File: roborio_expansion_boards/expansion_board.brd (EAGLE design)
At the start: 55.9 x 88.9 mm, 19 parts

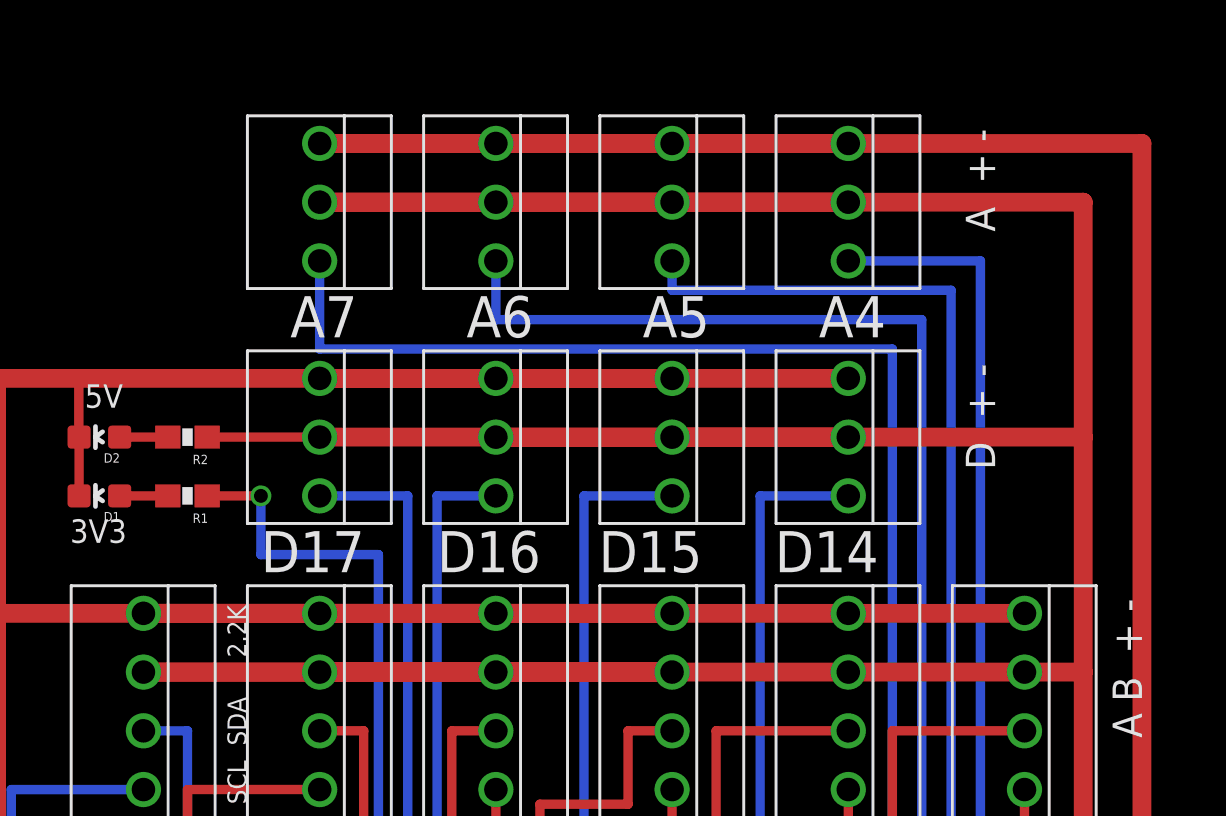
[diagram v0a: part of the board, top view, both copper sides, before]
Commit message: added capacitors to the power lines near each connector
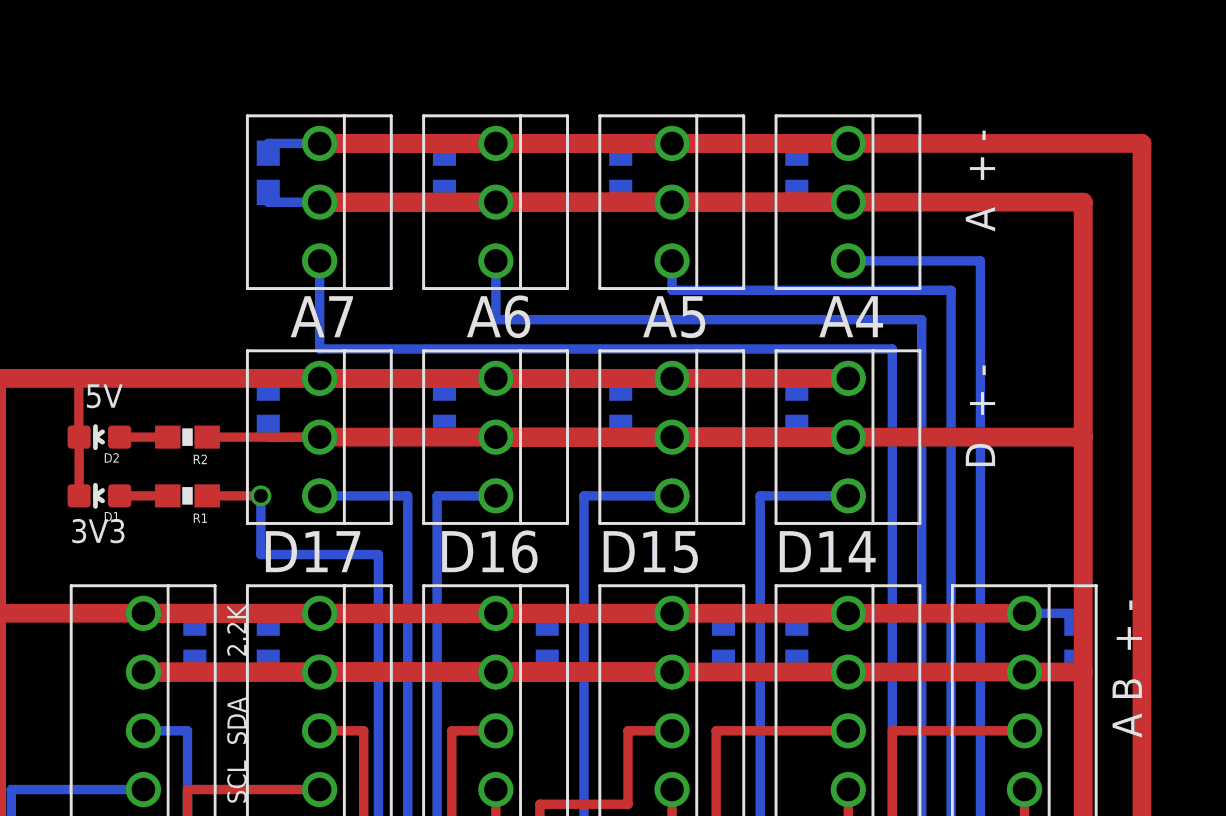
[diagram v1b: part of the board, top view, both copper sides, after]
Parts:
- added C1, C10, C11, C12, C13, C14, C2, C3, C4, C5, C6, C7, C8, C9: (no value), custom:0603
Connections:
- net 5V: now also C1.1, C10.2, C11.2, C12.2, C13.2, C14.2, C2.1, C3.1, C4.1, C5.1, C6.1, C7.2, C8.2, C9.2
- net AGND: now also C11.1, C12.1, C13.1, C14.1
- net DGND: now also C1.2, C10.1, C2.2, C3.2, C4.2, C5.2, C6.2, C7.1, C8.1, C9.1
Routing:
- net 5V: track 246.2 -> 283.2 mm
- net DGND: track 241.9 -> 268.4 mm
- net AGND: track 127.0 -> 137.6 mm
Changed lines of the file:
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@@
 <setting verticaltext="up"/>
 </settings>
-<grid distance="0.025" unitdist="inch" unit="inch" style="lines" multiple="1" display="no" altdistance="0.001" altunitdist="inch" altunit="inch"/>
+<grid distance="0.0125" unitdist="inch" unit="inch" style="lines" multiple="1" display="no" altdistance="0.001" altunitdist="inch" altunit="inch"/>
 <layers>
 <layer number="1" name="Top" color="4" fill="1" visible="yes" active="yes"/>
@@
 </element>
 <element name="R2" library="SparkFun-Passives" package="0603-RES" value="150" x="10.795" y="34.29" rot="R180"/>
+<element name="C1" library="custom" package="0603" value="" x="49.2125" y="25.4" rot="MR90"/>
+<element name="C2" library="custom" package="0603" value="" x="37.1475" y="25.4" rot="MR90"/>
+<element name="C3" library="custom" package="0603" value="" x="33.9725" y="25.4" rot="MR90"/>
+<element name="C4" library="custom" package="0603" value="" x="26.3525" y="25.4" rot="MR90"/>
+<element name="C5" library="custom" package="0603" value="" x="14.2875" y="25.4" rot="MR90"/>
+<element name="C6" library="custom" package="0603" value="" x="11.1125" y="25.4" rot="MR90"/>
+<element name="C7" library="custom" package="0603" value="" x="14.2875" y="35.56" rot="MR270"/>
+<element name="C8" library="custom" package="0603" value="" x="21.9075" y="35.56" rot="MR270"/>
+<element name="C9" library="custom" package="0603" value="" x="29.5275" y="35.56" rot="MR270"/>
+<element name="C10" library="custom" package="0603" value="" x="37.1475" y="35.56" rot="MR270"/>
+<element name="C11" library="custom" package="0603" value="" x="37.1475" y="45.72" rot="MR270"/>
+<element name="C12" library="custom" package="0603" value="" x="29.5275" y="45.72" rot="MR270"/>
+<element name="C13" library="custom" package="0603" value="" x="21.9075" y="45.72" rot="MR270"/>
+<element name="C14" library="custom" package="0603" value="" x="14.2875" y="45.72" rot="MR270"/>
 </elements>
 <signals>
@@
 <contactref element="R2" pad="1"/>
 <wire x1="11.645" y1="34.29" x2="16.51" y2="34.29" width="0.4064" layer="1"/>
+<contactref element="C1" pad="1"/>
+<contactref element="C2" pad="1"/>
+<contactref element="C3" pad="1"/>
+<contactref element="C4" pad="1"/>
+<contactref element="C5" pad="1"/>
+<contactref element="C6" pad="1"/>
+<wire x1="49.2125" y1="24.55" x2="49.2125" y2="24.13" width="0.4064" layer="16"/>
+<wire x1="49.2125" y1="24.13" x2="46.99" y2="24.13" width="0.4064" layer="16"/>
+<wire x1="37.1475" y1="24.55" x2="37.1475" y2="24.13" width="0.4064" layer="16"/>
+<wire x1="37.1475" y1="24.13" x2="39.37" y2="24.13" width="0.4064" layer="16"/>
+<wire x1="33.9725" y1="24.55" x2="33.9725" y2="24.13" width="0.4064" layer="16"/>
+<wire x1="33.9725" y1="24.13" x2="31.75" y2="24.13" width="0.4064" layer="16"/>
+<wire x1="26.3525" y1="24.55" x2="26.3525" y2="24.13" width="0.4064" layer="16"/>
+<wire x1="26.3525" y1="24.13" x2="24.13" y2="24.13" width="0.4064" layer="16"/>
+<wire x1="14.2875" y1="24.55" x2="14.2875" y2="24.13" width="0.4064" layer="16"/>
+<wire x1="14.2875" y1="24.13" x2="16.51" y2="24.13" width="0.4064" layer="16"/>
+<wire x1="11.1125" y1="24.55" x2="11.1125" y2="24.13" width="0.4064" layer="16"/>
+<wire x1="11.1125" y1="24.13" x2="8.89" y2="24.13" width="0.4064" layer="16"/>
+<contactref element="C7" pad="2"/>
+<contactref element="C8" pad="2"/>
+<contactref element="C9" pad="2"/>
+<contactref element="C10" pad="2"/>
+<wire x1="14.2875" y1="34.71" x2="14.2875" y2="34.29" width="0.4064" layer="16"/>
+<wire x1="14.2875" y1="34.29" x2="16.51" y2="34.29" width="0.4064" layer="16"/>
+<wire x1="21.9075" y1="34.71" x2="21.9075" y2="34.29" width="0.4064" layer="16"/>
+<wire x1="21.9075" y1="34.29" x2="24.13" y2="34.29" width="0.4064" layer="16"/>
+<wire x1="29.5275" y1="34.71" x2="29.5275" y2="34.29" width="0.4064" layer="16"/>
+<wire x1="29.5275" y1="34.29" x2="31.75" y2="34.29" width="0.4064" layer="16"/>
+<wire x1="37.1475" y1="34.71" x2="37.1475" y2="34.29" width="0.4064" layer="16"/>
+<wire x1="37.1475" y1="34.29" x2="39.37" y2="34.29" width="0.4064" layer="16"/>
+<contactref element="C11" pad="2"/>
+<contactref element="C12" pad="2"/>
+<contactref element="C13" pad="2"/>
+<contactref element="C14" pad="2"/>
+<wire x1="14.2875" y1="44.87" x2="14.2875" y2="44.45" width="0.4064" layer="16"/>
+<wire x1="14.2875" y1="44.45" x2="16.51" y2="44.45" width="0.4064" layer="16"/>
+<wire x1="21.9075" y1="44.87" x2="21.9075" y2="44.45" width="0.4064" layer="16"/>
+<wire x1="21.9075" y1="44.45" x2="24.13" y2="44.45" width="0.4064" layer="16"/>
+<wire x1="29.5275" y1="44.87" x2="29.5275" y2="44.45" width="0.4064" layer="16"/>
+<wire x1="29.5275" y1="44.45" x2="31.75" y2="44.45" width="0.4064" layer="16"/>
+<wire x1="37.1475" y1="44.87" x2="37.1475" y2="44.45" width="0.4064" layer="16"/>
+<wire x1="37.1475" y1="44.45" x2="39.37" y2="44.45" width="0.4064" layer="16"/>
 </signal>
 <signal name="DGND">
@@
 <wire x1="6.108" y1="34.29" x2="6.096" y2="34.29" width="0.4064" layer="1"/>
 <wire x1="6.096" y1="34.29" x2="6.096" y2="36.83" width="0.4064" layer="1"/>
+<contactref element="C1" pad="2"/>
+<contactref element="C2" pad="2"/>
+<contactref element="C3" pad="2"/>
+<contactref element="C4" pad="2"/>
+<contactref element="C5" pad="2"/>
+<contactref element="C6" pad="2"/>
+<wire x1="49.2125" y1="26.25" x2="49.2125" y2="26.67" width="0.4064" layer="16"/>
+<wire x1="49.2125" y1="26.67" x2="46.99" y2="26.67" width="0.4064" layer="16"/>
+<wire x1="37.1475" y1="26.25" x2="37.1475" y2="26.67" width="0.4064" layer="16"/>
+<wire x1="37.1475" y1="26.67" x2="39.37" y2="26.67" width="0.4064" layer="16"/>
+<wire x1="33.9725" y1="26.25" x2="33.9725" y2="26.67" width="0.4064" layer="16"/>
+<wire x1="33.9725" y1="26.67" x2="31.75" y2="26.67" width="0.4064" layer="16"/>
+<wire x1="26.3525" y1="26.25" x2="26.3525" y2="26.67" width="0.4064" layer="16"/>
+<wire x1="26.3525" y1="26.67" x2="24.13" y2="26.67" width="0.4064" layer="16"/>
+<wire x1="14.2875" y1="26.25" x2="14.2875" y2="26.67" width="0.4064" layer="16"/>
+<wire x1="14.2875" y1="26.67" x2="16.51" y2="26.67" width="0.4064" layer="16"/>
+<wire x1="11.1125" y1="26.25" x2="11.1125" y2="26.67" width="0.4064" layer="16"/>
+<wire x1="11.1125" y1="26.67" x2="8.89" y2="26.67" width="0.4064" layer="16"/>
+<contactref element="C7" pad="1"/>
+<contactref element="C8" pad="1"/>
+<contactref element="C9" pad="1"/>
+<contactref element="C10" pad="1"/>
+<wire x1="14.2875" y1="36.41" x2="14.2875" y2="36.83" width="0.4064" layer="16"/>
+<wire x1="14.2875" y1="36.83" x2="16.51" y2="36.83" width="0.4064" layer="16"/>
+<wire x1="21.9075" y1="36.41" x2="21.9075" y2="36.83" width="0.4064" layer="16"/>
+<wire x1="21.9075" y1="36.83" x2="24.13" y2="36.83" width="0.4064" layer="16"/>
+<wire x1="29.5275" y1="36.41" x2="29.5275" y2="36.83" width="0.4064" layer="16"/>
+<wire x1="29.5275" y1="36.83" x2="31.75" y2="36.83" width="0.4064" layer="16"/>
+<wire x1="37.1475" y1="36.41" x2="37.1475" y2="36.83" width="0.4064" layer="16"/>
+<wire x1="37.1475" y1="36.83" x2="39.37" y2="36.83" width="0.4064" layer="16"/>
 </signal>
 <signal name="N$9">
@@
 <wire x1="52.07" y1="5.08" x2="43.18" y2="5.08" width="0.8128" layer="1"/>
 <wire x1="43.18" y1="5.08" x2="43.18" y2="7.62" width="0.8128" layer="1"/>
+<contactref element="C11" pad="1"/>
+<contactref element="C12" pad="1"/>
+<contactref element="C13" pad="1"/>
+<contactref element="C14" pad="1"/>
+<wire x1="14.2875" y1="46.57" x2="14.2875" y2="46.99" width="0.4064" layer="16"/>
+<wire x1="14.2875" y1="46.99" x2="16.51" y2="46.99" width="0.4064" layer="16"/>
+<wire x1="21.9075" y1="46.57" x2="21.9075" y2="46.99" width="0.4064" layer="16"/>
+<wire x1="21.9075" y1="46.99" x2="24.13" y2="46.99" width="0.4064" layer="16"/>
+<wire x1="29.5275" y1="46.57" x2="29.5275" y2="46.99" width="0.4064" layer="16"/>
+<wire x1="29.5275" y1="46.99" x2="31.75" y2="46.99" width="0.4064" layer="16"/>
+<wire x1="37.1475" y1="46.57" x2="37.1475" y2="46.99" width="0.4064" layer="16"/>
+<wire x1="37.1475" y1="46.99" x2="39.37" y2="46.99" width="0.4064" layer="16"/>
 </signal>
 <signal name="N$17">

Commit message: finish PCBs and generate Gerbers for Seeed
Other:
- board size 55.9 x 88.9 mm -> 55.9 x 81.9 mm
- board text added: "FRC Team 971 MXP Breakout 20140818"
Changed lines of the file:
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@@
 <plain>
 <wire x1="0" y1="0" x2="55.88" y2="0" width="0" layer="20"/>
-<wire x1="55.88" y1="0" x2="55.88" y2="88.9" width="0" layer="20"/>
-<wire x1="55.88" y1="88.9" x2="0" y2="88.9" width="0" layer="20"/>
-<wire x1="0" y1="88.9" x2="0" y2="0" width="0" layer="20"/>
+<wire x1="55.88" y1="0" x2="55.88" y2="81.915" width="0" layer="20"/>
+<wire x1="55.88" y1="81.915" x2="0" y2="81.915" width="0" layer="20"/>
+<wire x1="0" y1="81.915" x2="0" y2="0" width="0" layer="20"/>
 <text x="44.45" y="37.465" size="1.27" layer="21" rot="R270">D  + -</text>
 <text x="44.45" y="47.625" size="1.27" layer="21" rot="R270">A  + -</text>
@@
 <text x="5.715" y="29.718" size="1.016" layer="21">3V3</text>
 <text x="13.335" y="20.955" size="0.8128" layer="21" rot="R90">SDA</text>
+<text x="20.955" y="1.5875" size="0.6096" layer="1" font="vector">FRC Team 971 MXP Breakout
+20140818</text>
+<text x="9.525" y="50.165" size="1.778" layer="1" font="vector">FRC Team 971 MXP Breakout
+20140818</text>
+<text x="9.525" y="69.85" size="1.778" layer="1" font="vector">FRC Team 971 MXP Breakout
+20140818</text>
 </plain>
 <attributes>
@@
 </signal>
 <signal name="N$21">
-<via x="3.1242" y="55.88" extent="1-16" drill="3.175"/>
+<via x="3.1242" y="78.1685" extent="1-16" drill="3.2"/>
 </signal>
 <signal name="N$22">
-<via x="52.7558" y="55.88" extent="1-16" drill="3.175"/>
+<via x="52.7558" y="78.1685" extent="1-16" drill="3.2"/>
 </signal>
 <signal name="N$23">
@@
 </signal>
 </signals>
+<errors>
+</errors>
 </board>
 </drawing>
+<compatibility>
+<note version="6.3" minversion="6.2.2" severity="warning">
+Since Version 6.2.2 text objects can contain more than one line,
+which will not be processed correctly with this version.
+</note>
+</compatibility>
 </eagle>
